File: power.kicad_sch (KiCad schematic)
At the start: 158 parts, among them Q10 SI7613DN-T1-GE3, Q2 BC817-25W, Q3 DZDH0401DW, Q4 DZDH0401DW, Q5 SI7613DN-T1-GE3, Q6 SI7613DN-T1-GE3, Q8 BC817-25W, U1 LT8350RV#PBF, U10 LM3881MME_NOPB, U11 AP22615A_TSOT26, U2 MP2386GG, U3 TPS65983BAZBHR, U9 LM1117MP-3.3_NOPB

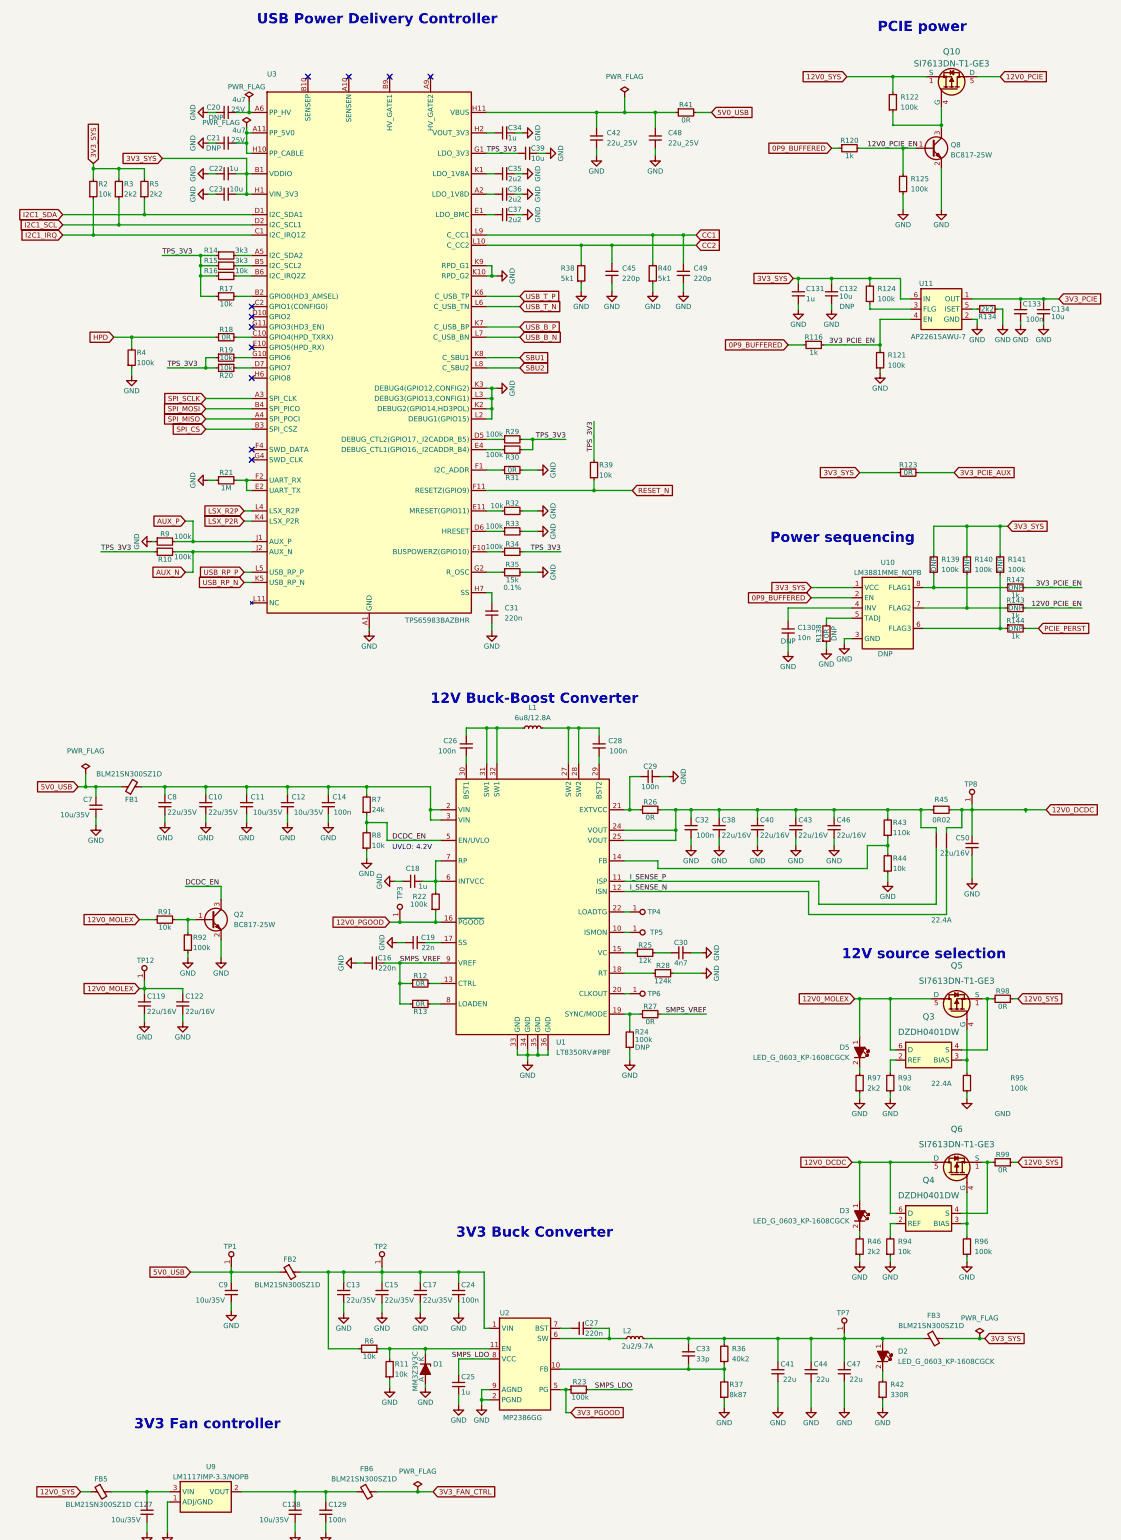
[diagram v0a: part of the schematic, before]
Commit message: Add filtration to PD controller
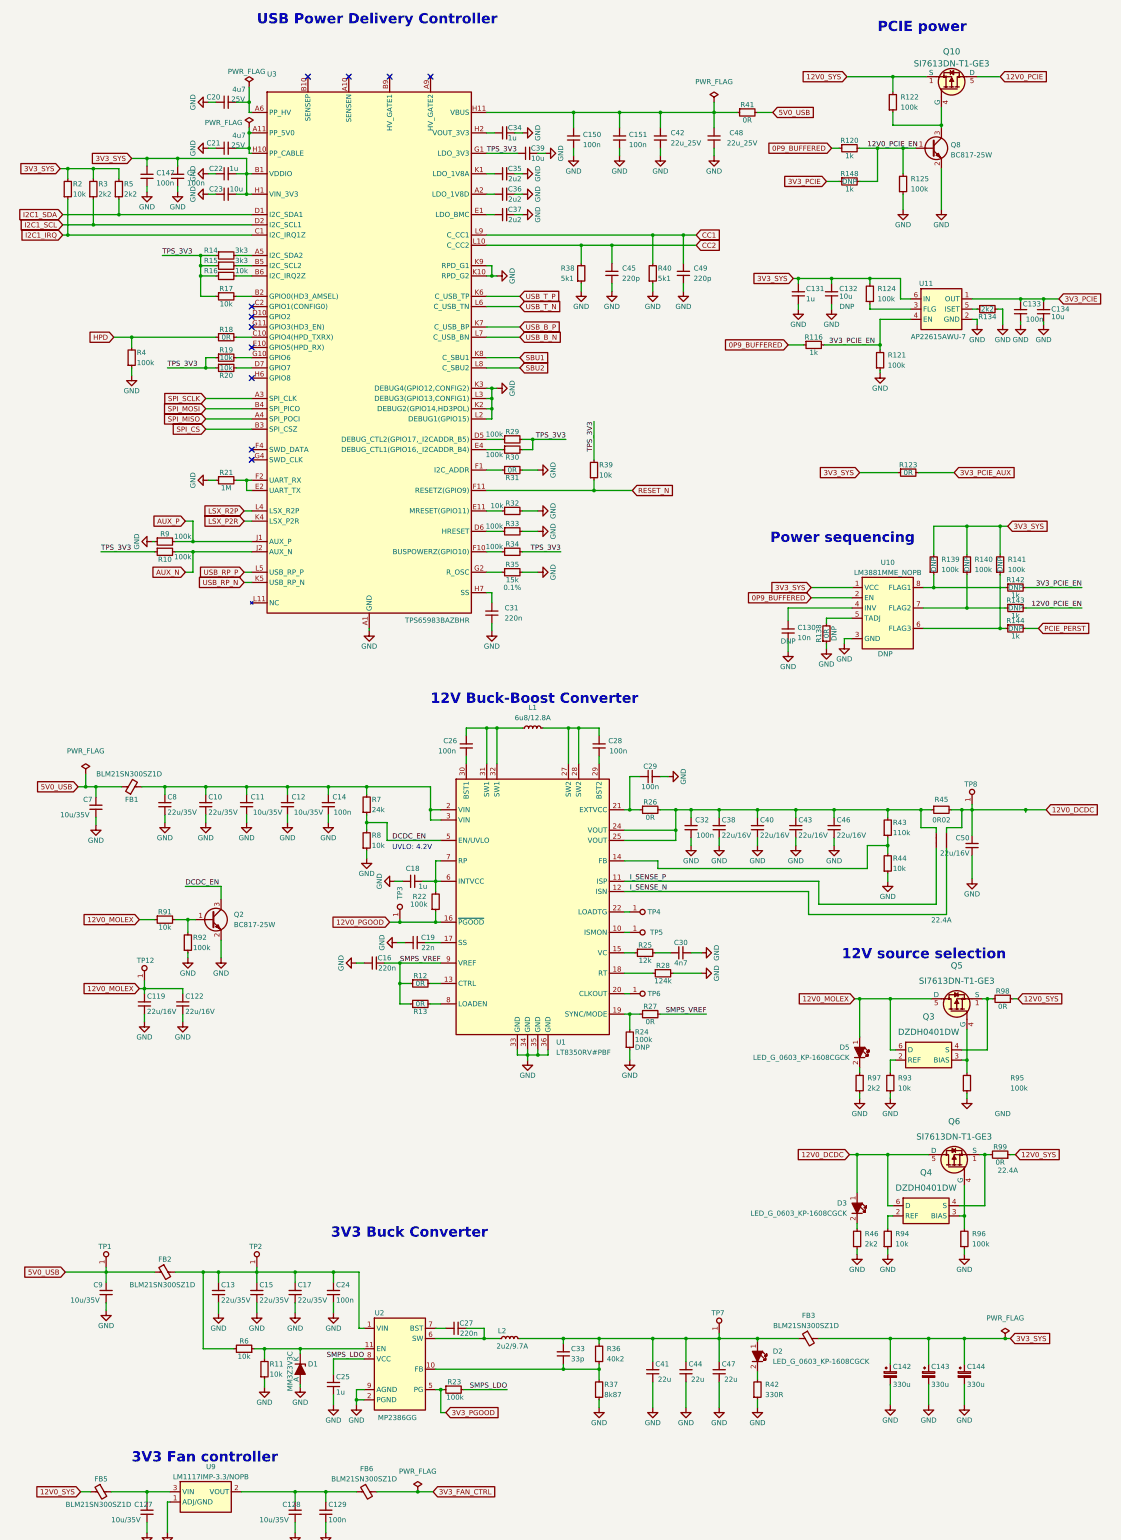
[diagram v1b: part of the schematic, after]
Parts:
- added C142, C143, C144: C_330u_KEMET_B, thunderbolt-gpu-adapter-footprints:KEMET_B, symbol thunderbolt-gpu-adapter:C_330u_KEMET_B
- added C147, C150, C151, C?: C_100n_0402, antmicro-footprints:C_0402_1005Metric, symbol antmicroCapacitors0402:C_100n_0402
- added R148: R_1k_0402, thunderbolt-gpu-adapter-footprints:R_0402_1005Metric, symbol thunderbolt-gpu-adapter:R_1k_0402
- C20, C21: DNP DNP -> (none)
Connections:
- net 12V0_PCIE_EN: now also R148.2
- net 3V3_PCIE: now also R148.1
- net 3V3_SYS: now also C142.1, C143.1, C144.1, C147.2, C?.2
- net GND: now also C142.2, C143.2, C144.2, C147.1, C150.1, C151.1, C?.1
- net VBUS: now also C150.2, C151.2
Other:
- moved on the sheet: C13, C15, C17, C20, C21, C24, C25, C27, C33, C41, C42, C44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

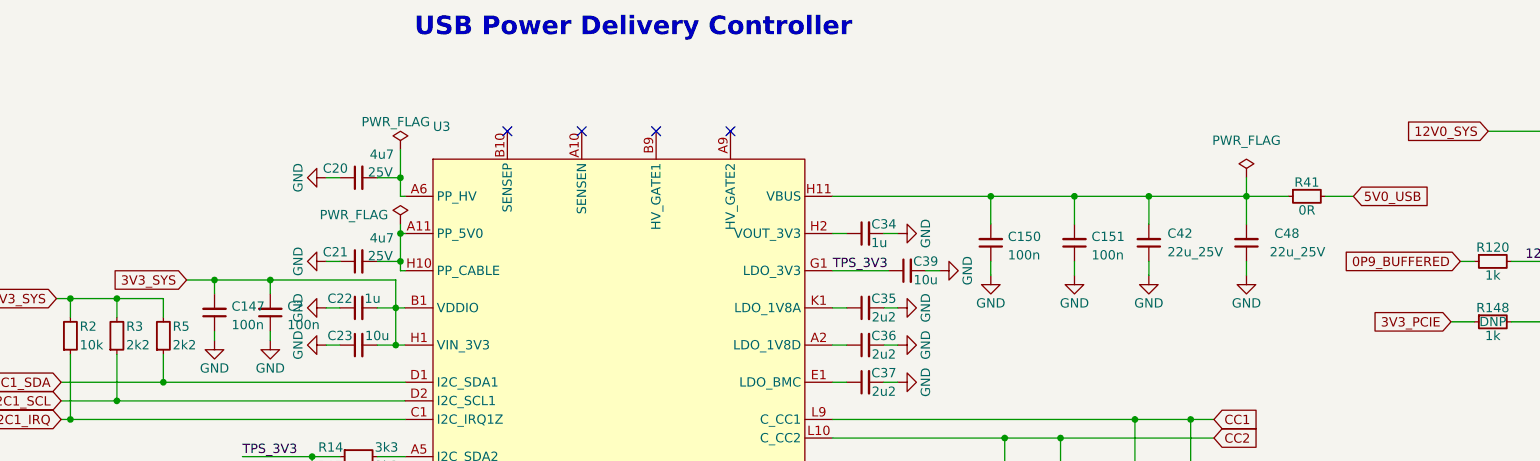
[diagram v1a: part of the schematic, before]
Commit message: Improved power filtration for TB controller
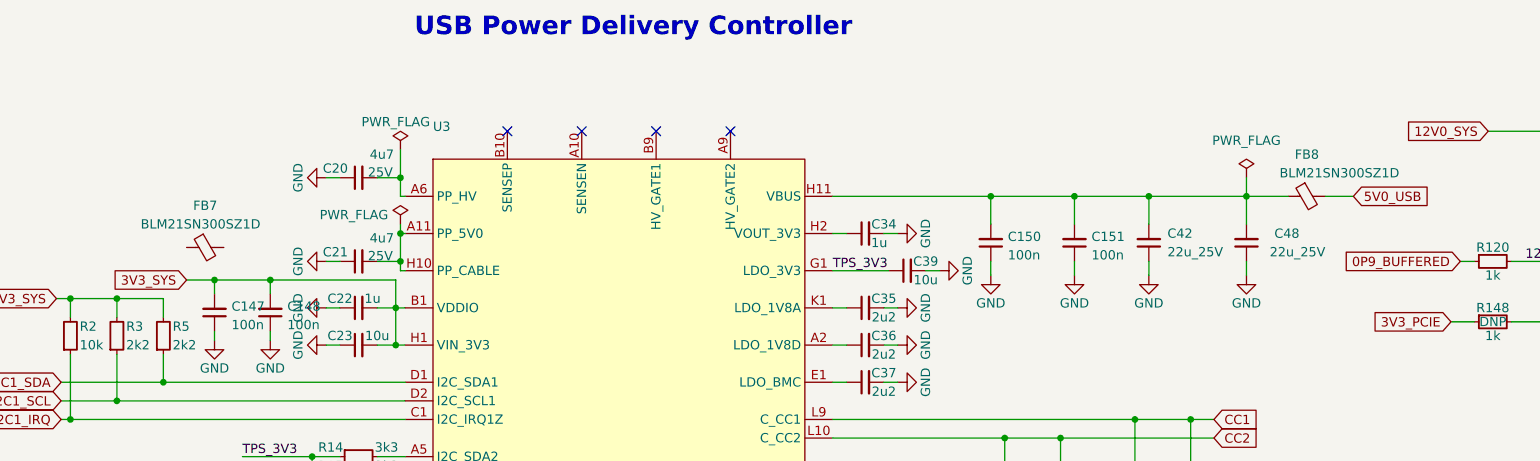
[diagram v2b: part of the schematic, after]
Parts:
- removed R41: R_0R_0603, thunderbolt-gpu-adapter-footprints:R_0603_1608Metric, symbol thunderbolt-gpu-adapter:R_0R_0603
- added FB7, FB8: BLM21SN300SZ1D, thunderbolt-gpu-adapter-footprints:FB_0805_2012Metric, symbol thunderbolt-gpu-adapter:BLM21SN300SZ1D
- gave numbers to parts that had none: 1
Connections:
- net 5V0_USB: now also FB8.2
- net VBUS: now also FB8.1
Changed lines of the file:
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@@
     (pin "1")
   )
-  (symbol (lib_id "thunderbolt-gpu-adapter:R_0R_0603") (at 193.675 41.91 0) (unit 1)
-    (in_bom yes) (on_board yes)
-    (property "Reference" "R41" (id 0) (at 196.215 40.005 0)
-      (effects (font (size 1.27 1.27) (thickness 0.15)))
-    )
-    (property "Value" "R_0R_0603" (id 1) (at 213.995 54.61 0)
-      (effects (font (size 1.27 1.27) (thickness 0.15)) (justify left bottom) hide)
-    )
-    (property "Footprint" "thunderbolt-gpu-adapter-footprints:R_0603_1608Metric" (id 2) (at 213.995 57.15 0)
-      (effects (font (size 1.27 1.27) (thickness 0.15)) (justify left bottom) hide)
-    )
-    (property "Datasheet" "https://www.bourns.com/docs/product-datasheets/cr.pdf?sfvrsn=574d41f6_14" (id 3) (at 213.995 59.69 0)
-      (effects (font (size 1.27 1.27) (thickness 0.15)) (justify left bottom) hide)
-    )
-    (property "MPN" "CR0603-J/-000ELF" (id 4) (at 213.995 62.23 0)
-      (effects (font (size 1.27 1.27) (thickness 0.15)) (justify left bottom) hide)
-    )
-    (property "Manufacturer" "Bourns" (id 5) (at 213.995 64.77 0)
-      (effects (font (size 1.27 1.27) (thickness 0.15)) (justify left bottom) hide)
-    )
-    (property "License" "Apache-2.0" (id 6) (at 213.995 67.31 0)
-      (effects (font (size 1.27 1.27) (thickness 0.15)) (justify left bottom) hide)
-    )
-    (property "Val" "0R" (id 8) (at 196.215 43.815 0)
-      (effects (font (size 1.27 1.27) (thickness 0.15)))
-    )
-    (property "Tolerance" "~" (id 9) (at 213.995 52.07 0)
-      (effects (font (size 1.27 1.27)) (justify left bottom) hide)
-    )
-    (property "Current" "1A" (id 10) (at 196.215 38.735 0)
-      (effects (font (size 1.27 1.27) (thickness 0.15)) hide)
-    )
-    (property "Author" "Antmicro" (id 11) (at 213.995 69.85 0)
-      (effects (font (size 1.27 1.27) (thickness 0.15)) (justify left bottom) hide)
-    )
-    (pin "1")
-    (pin "2")
-  )
   (symbol (lib_name "C_100n_0402_7") (lib_id "thunderbolt-gpu-adapter:C_100n_0402") (at 126.365 201.93 90) (unit 1)
     (in_bom yes) (on_board yes)
@@
     (pin "1")
   )
+  (symbol (lib_id "thunderbolt-gpu-adapter:BLM21SN300SZ1D") (at 193.675 41.91 0) (mirror x) (unit 1)
+    (in_bom yes) (on_board yes)
+    (property "Reference" "FB8" (id 0) (at 196.215 36.195 0)
+      (effects (font (size 1.27 1.27) (thickness 0.15)))
+    )
+    (property "Value" "BLM21SN300SZ1D" (id 1) (at 200.66 38.735 0)
+      (effects (font (size 1.27 1.27) (thickness 0.15)))
+    )
+    (property "Footprint" "thunderbolt-gpu-adapter-footprints:FB_0805_2012Metric" (id 2) (at 207.645 36.83 0)
+      (effects (font (size 1.27 1.27) (thickness 0.15)) (justify left bottom) hide)
+    )
+    (property "Datasheet" "https://www.murata.com/en-sg/products/productdata/8796738977822/ENFA0005.pdf?1519270210000" (id 3) (at 207.645 34.29 0)
+      (effects (font (size 1.27 1.27) (thickness 0.15)) (justify left bottom) hide)
+    )
+    (property "MPN" "BLM21SN300SZ1D" (id 4) (at 207.645 31.75 0)
+      (effects (font (size 1.27 1.27) (thickness 0.15)) (justify left bottom) hide)
+    )
+    (property "Manufacturer" "Murata" (id 5) (at 207.645 29.21 0)
+      (effects (font (size 1.27 1.27) (thickness 0.15)) (justify left bottom) hide)
+    )
+    (property "License" "Apache-2.0" (id 7) (at 207.645 24.13 0)
+      (effects (font (size 1.27 1.27) (thickness 0.15)) (justify left bottom) hide)
+    )
+    (property "Author" "Antmicro" (id 8) (at 207.645 26.67 0)
+      (effects (font (size 1.27 1.27) (thickness 0.15)) (justify left bottom) hide)
+    )
+    (pin "1")
+    (pin "2")
+  )
   (symbol (lib_id "thunderbolt-gpu-adapter:GND") (at 65.405 252.095 0) (unit 1)
     (in_bom yes) (on_board yes)
@@
   (symbol (lib_id "antmicroCapacitors0402:C_100n_0402") (at 54.61 60.325 90) (unit 1)
     (in_bom yes) (on_board yes) (fields_autoplaced)
-    (property "Reference" "C?" (id 0) (at 56.9341 56.948 90)
+    (property "Reference" "C148" (id 0) (at 56.9341 56.948 90)
       (effects (font (size 1.27 1.27) (thickness 0.15)) (justify right))
     )
@@
   (symbol (lib_id "thunderbolt-gpu-adapter:GND") (at 54.61 61.595 0) (unit 1)
     (in_bom yes) (on_board yes)
-    (property "Reference" "#PWR?" (id 0) (at 54.61 67.945 0)
+    (property "Reference" "#PWR0220" (id 0) (at 54.61 67.945 0)
       (effects (font (size 1.27 1.27)) hide)
     )
@@
       (effects (font (size 1.27 1.27) (thickness 0.15)) (justify left bottom) hide)
     )
+    (pin "1")
+    (pin "2")
+  )
+  (symbol (lib_id "thunderbolt-gpu-adapter:BLM21SN300SZ1D") (at 43.18 48.895 0) (mirror x) (unit 1)
+    (in_bom yes) (on_board yes)
+    (property "Reference" "FB7" (id 0) (at 45.72 43.18 0)
+      (effects (font (size 1.27 1.27) (thickness 0.15)))
+    )
+    (property "Value" "BLM21SN300SZ1D" (id 1) (at 45.085 45.72 0)
+      (effects (font (size 1.27 1.27) (thickness 0.15)))
+    )
+    (property "Footprint" "thunderbolt-gpu-adapter-footprints:FB_0805_2012Metric" (id 2) (at 57.15 43.815 0)
+      (effects (font (size 1.27 1.27) (thickness 0.15)) (justify left bottom) hide)
+    )
+    (property "Datasheet" "https://www.murata.com/en-sg/products/productdata/8796738977822/ENFA0005.pdf?1519270210000" (id 3) (at 57.15 41.275 0)
+      (effects (font (size 1.27 1.27) (thickness 0.15)) (justify left bottom) hide)
+    )
+    (property "MPN" "BLM21SN300SZ1D" (id 4) (at 57.15 38.735 0)
+      (effects (font (size 1.27 1.27) (thickness 0.15)) (justify left bottom) hide)
+    )
+    (property "Manufacturer" "Murata" (id 5) (at 57.15 36.195 0)
+      (effects (font (size 1.27 1.27) (thickness 0.15)) (justify left bottom) hide)
+    )
+    (property "License" "Apache-2.0" (id 7) (at 57.15 31.115 0)
+      (effects (font (size 1.27 1.27) (thickness 0.15)) (justify left bottom) hide)
+    )
+    (property "Author" "Antmicro" (id 8) (at 57.15 33.655 0)
+      (effects (font (size 1.27 1.27) (thickness 0.15)) (justify left bottom) hide)
+    )

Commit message: WIP Working on layout of the PCIe power
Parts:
- removed C142, C143, C144: C_330u_KEMET_B, thunderbolt-gpu-adapter-footprints:KEMET_B, symbol thunderbolt-gpu-adapter:C_330u_KEMET_B
- added C141, C142, C143: C_Pol_330u_6.3V_KEMET-T520-B, antmicro-footprints:C_Pol_EIA-B, symbol antmicroCapacitorspol:C_Pol_330u_6.3V_KEMET-T520-B
- added C? (x2): C_Pol_330u_16V_KYOCERA-AVX-TCJ-E, antmicro-footprints:C_Pol_EIA-E, symbol antmicroCapacitorspol:C_Pol_330u_16V_KYOCERA-AVX-TCJ-E
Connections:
- net 12V0_SYS: now also C?.1, C?.1
- net 3V3_SYS: now also C141.1, C142.1, C143.1
- net GND: now also C141.2, C142.2, C143.2, C?.2, C?.2

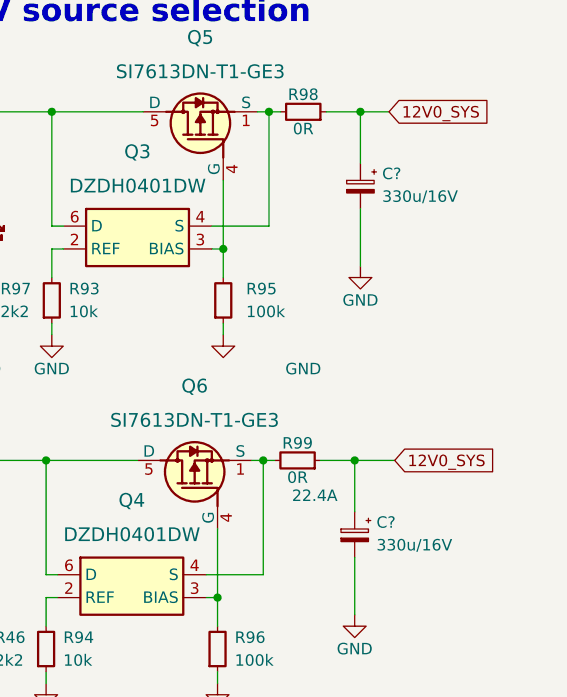
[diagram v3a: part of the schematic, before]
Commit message: Added filtration for 3V3_SYS, 12V0_SYS, 3V3_PCIE, 12V0_PCIE
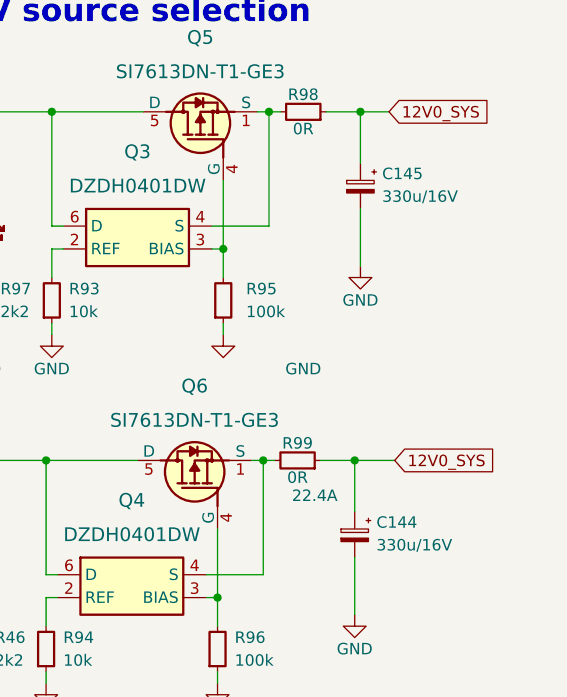
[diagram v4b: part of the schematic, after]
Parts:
- gave numbers to parts that had none: 2
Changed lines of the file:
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@@
   (symbol (lib_id "thunderbolt-gpu-adapter:GND") (at 265.43 318.135 0) (unit 1)
     (in_bom yes) (on_board yes)
-    (property "Reference" "#PWR?" (id 0) (at 265.43 324.485 0)
+    (property "Reference" "#PWR0213" (id 0) (at 265.43 324.485 0)
       (effects (font (size 1.27 1.27)) hide)
     )
@@
   (symbol (lib_id "antmicroCapacitorspol:C_Pol_330u_16V_KYOCERA-AVX-TCJ-E") (at 265.43 306.705 270) (unit 1)
     (in_bom yes) (on_board yes) (fields_autoplaced)
-    (property "Reference" "C?" (id 0) (at 267.843 307.881 90)
+    (property "Reference" "C144" (id 0) (at 267.843 307.881 90)
       (effects (font (size 1.27 1.27) (thickness 0.15)) (justify left))
     )
@@
   (symbol (lib_id "antmicroCapacitorspol:C_Pol_330u_16V_KYOCERA-AVX-TCJ-E") (at 266.065 267.97 270) (unit 1)
     (in_bom yes) (on_board yes) (fields_autoplaced)
-    (property "Reference" "C?" (id 0) (at 268.478 269.146 90)
+    (property "Reference" "C145" (id 0) (at 268.478 269.146 90)
       (effects (font (size 1.27 1.27) (thickness 0.15)) (justify left))
     )
@@
   (symbol (lib_id "thunderbolt-gpu-adapter:GND") (at 266.065 279.4 0) (unit 1)
     (in_bom yes) (on_board yes)
-    (property "Reference" "#PWR?" (id 0) (at 266.065 285.75 0)
+    (property "Reference" "#PWR0224" (id 0) (at 266.065 285.75 0)
       (effects (font (size 1.27 1.27)) hide)
     )
